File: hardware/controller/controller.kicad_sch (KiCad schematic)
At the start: 6 parts, among them J1 SENSOR_LINK_2mm, J4 USB_STACK_4_1.27mm, J5 USB2_PIGTAIL_4_WIRES, U2 ADS1115 module

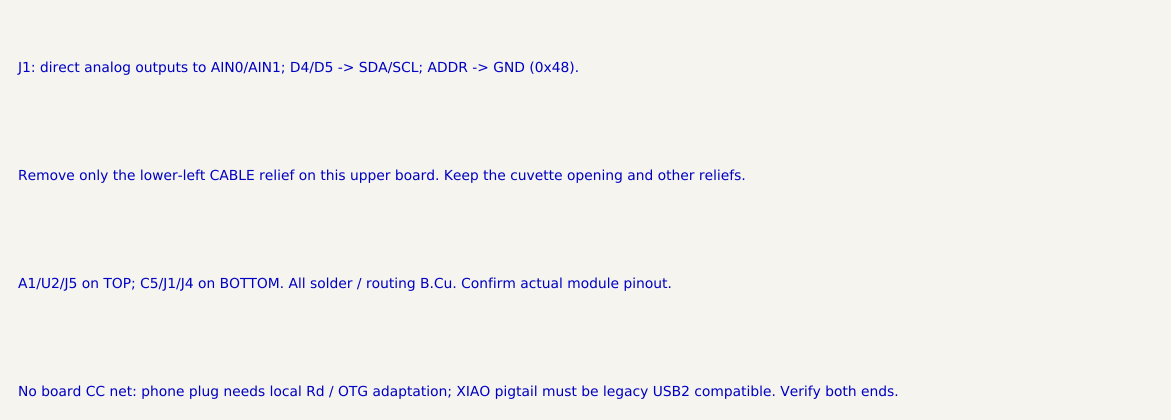
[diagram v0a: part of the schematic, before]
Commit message: Update 32 files (3D, docs, hardware, raíz)
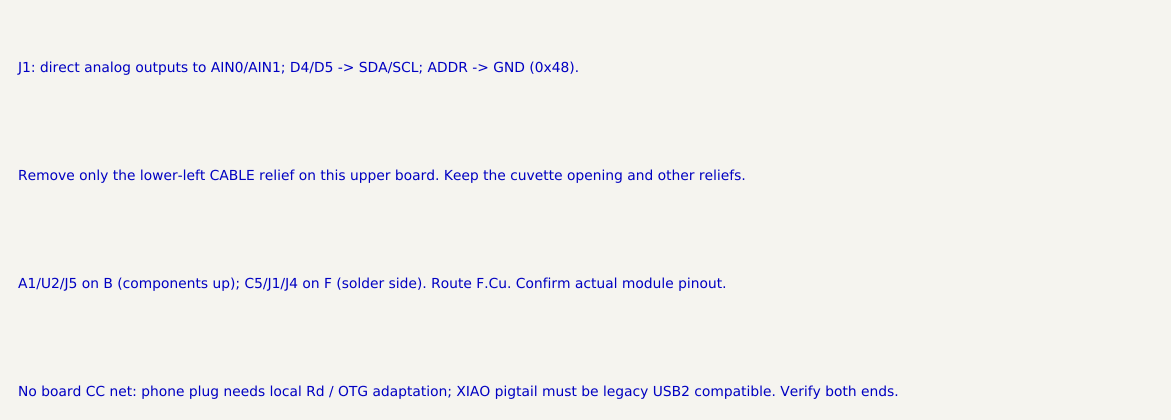
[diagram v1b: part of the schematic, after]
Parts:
- J4: footprint Connector_PinSocket_1.27mm:PinSocket_2x02_P1.27mm_Vertical_SMD -> Turbimeter:USB_StackSocket_2x02_P1.27mm_Upper_v10
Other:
- note added: "A1/U2/J5 on B (components up); C5/J1/J4 on F (solder side). Route F.Cu. Confirm actual module pinout."
- note removed: "A1/U2/J5 on TOP; C5/J1/J4 on BOTTOM. All solder / routing B.Cu. Confirm actual module pinout."

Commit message: Update 9 files (hardware)
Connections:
- net USB_DM: now also J5.1 (Pin_1); no longer J5.3 (Pin_3)
- net USB_VBUS: now also J5.3 (Pin_3); no longer J5.1 (Pin_1)
